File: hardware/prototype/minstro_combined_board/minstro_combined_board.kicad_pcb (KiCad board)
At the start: 4 copper layers, 130 x 100 mm, 89 parts, among them J301 BATT, J401 BOOT, J402 UART, J403 USB_C_Receptacle_USB2.0_16P, J404 SDMMC 4b, J405 Conn_Coaxial, J601 FT6236_Conn_01x06, J602 ILI9488_Conn, J603 ST7789_Conn_01x12, Q601 2N7002, SW401 RST, SW801 Navigation_Encoder_Joystick_S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, SW901 POWER, U201 LMR36006, U301 BQ24074RGT, U401 ESP32-S3, U402 W25Q128JVS, U701 ATSAMD10D13A-M, Y401 40 MHz

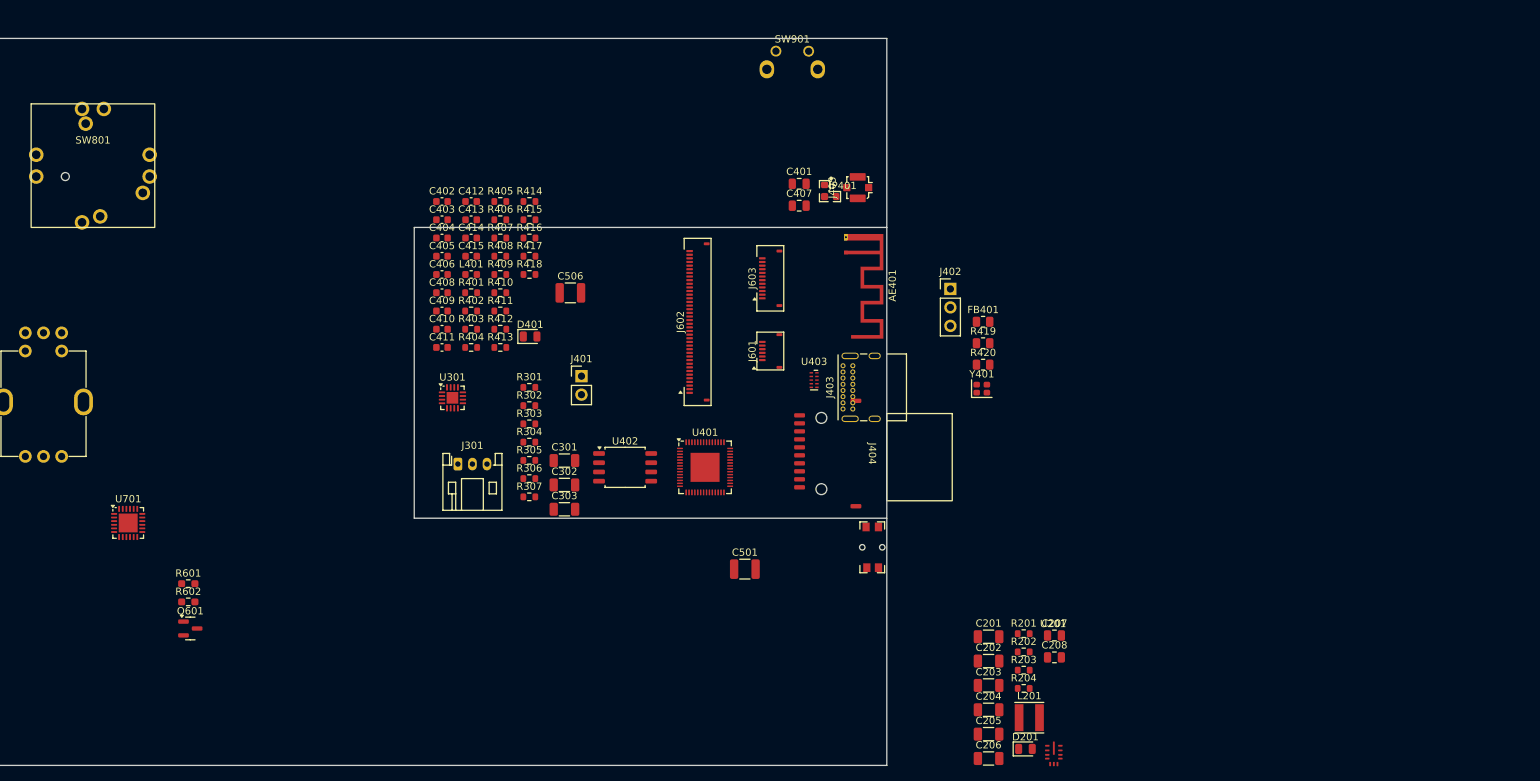
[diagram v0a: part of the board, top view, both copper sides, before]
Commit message: Footprint assignment and PCB layout work
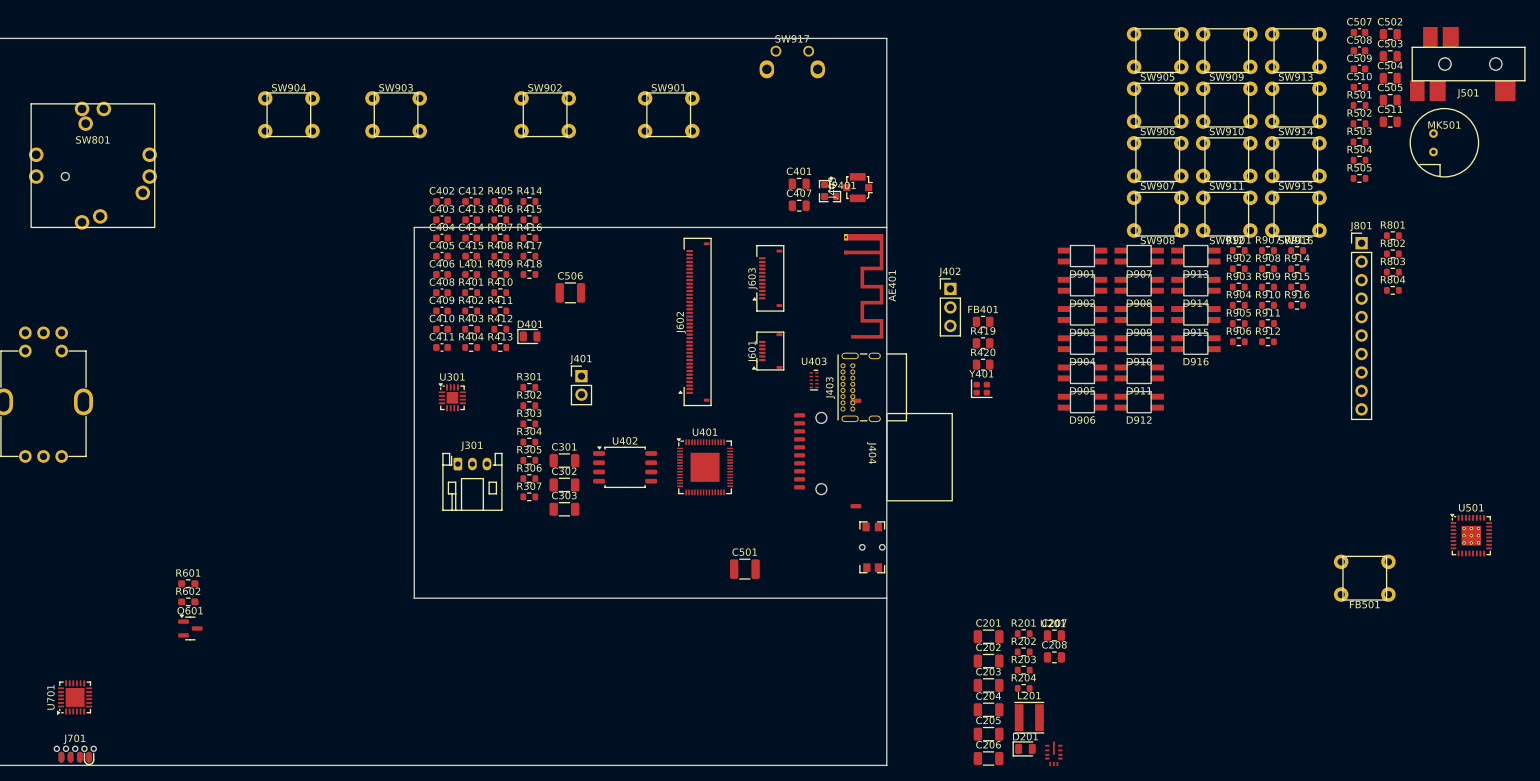
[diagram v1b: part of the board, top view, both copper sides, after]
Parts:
- added C502: 4.7uF, Capacitor_SMD:C_0805_2012Metric, F.Cu at (264.2, 39.4)
- added C503: 4.7uF, Capacitor_SMD:C_0805_2012Metric, F.Cu at (264.2, 42.4)
- added C504: 4.7uF, Capacitor_SMD:C_0805_2012Metric, F.Cu at (264.2, 45.5)
- added C505: 4.7uF, Capacitor_SMD:C_0805_2012Metric, F.Cu at (264.2, 48.5)
- added C507: 1uF, Capacitor_SMD:C_0603_1608Metric, F.Cu at (260.0, 39.2)
- added C508: 1uF, Capacitor_SMD:C_0603_1608Metric, F.Cu at (260.0, 41.7)
- added C509: 1uF, Capacitor_SMD:C_0603_1608Metric, F.Cu at (260.0, 44.2)
- added C510: 1uF, Capacitor_SMD:C_0603_1608Metric, F.Cu at (260.0, 46.7)
- added C511: 4.7uF, Capacitor_SMD:C_0805_2012Metric, F.Cu at (264.2, 51.5)
- added D901: ~, BVH_LED:SK6812Mini-E_Front, F.Cu at (221.9, 69.9)
- added D902: ~, BVH_LED:SK6812Mini-E_Front, F.Cu at (221.9, 74.0)
- added D903: ~, BVH_LED:SK6812Mini-E_Front, F.Cu at (221.9, 78.0)
- added D904: ~, BVH_LED:SK6812Mini-E_Front, F.Cu at (221.9, 82.0)
- added D905: ~, BVH_LED:SK6812Mini-E_Front, F.Cu at (221.9, 86.0)
- added D906: ~, BVH_LED:SK6812Mini-E_Front, F.Cu at (221.9, 90.0)
- added D907: ~, BVH_LED:SK6812Mini-E_Front, F.Cu at (229.7, 69.9)
- added D908: ~, BVH_LED:SK6812Mini-E_Front, F.Cu at (229.7, 74.0)
- added D909: ~, BVH_LED:SK6812Mini-E_Front, F.Cu at (229.7, 78.0)
- added D910: ~, BVH_LED:SK6812Mini-E_Front, F.Cu at (229.7, 82.0)
- added D911: ~, BVH_LED:SK6812Mini-E_Front, F.Cu at (229.7, 86.0)
- added D912: ~, BVH_LED:SK6812Mini-E_Front, F.Cu at (229.7, 90.0)
- added D913: ~, BVH_LED:SK6812Mini-E_Front, F.Cu at (237.5, 69.9)
- added D914: ~, BVH_LED:SK6812Mini-E_Front, F.Cu at (237.5, 74.0)
- added D915: ~, BVH_LED:SK6812Mini-E_Front, F.Cu at (237.5, 78.0)
- added D916: ~, BVH_LED:SK6812Mini-E_Front, F.Cu at (237.5, 82.0)
- added FB501: FerriteBead_Small, BVH_Switches:TacButton_6mm_6mm, F.Cu at (260.8, 114.2)
- added J501: Headset, BVH_Connectors_Misc:SJ-43515RS-SMT-TR, F.Cu at (275.0, 43.5)
- added J701: SOICbite-SWD, BVH_SOICbite:SOICbite_renumbered, F.Cu at (83.4, 140.0)
- added J801: Conn_01x10, Connector_PinHeader_2.54mm:PinHeader_1x10_P2.54mm_Vertical, F.Cu at (260.3, 68.2)
- added MK501: Microphone, BVH_Audio:SameSky_CMB-6544PF_Electret_Mic_9.4d, F.Cu at (271.7, 54.4)
- added R501: 100k, Resistor_SMD:R_0603_1608Metric, F.Cu at (260.0, 49.2)
- added R502: 100k, Resistor_SMD:R_0603_1608Metric, F.Cu at (260.0, 51.7)
- added R503: 220k, Resistor_SMD:R_0603_1608Metric, F.Cu at (260.0, 54.2)
- added R504: 2.2k, Resistor_SMD:R_0603_1608Metric, F.Cu at (260.0, 56.8)
- added R505: 2.2k, Resistor_SMD:R_0603_1608Metric, F.Cu at (260.0, 59.3)
- added R801: R_1, Resistor_SMD:R_0603_1608Metric, F.Cu at (264.6, 67.1)
- added R802: R_2, Resistor_SMD:R_0603_1608Metric, F.Cu at (264.6, 69.6)
- added R803: R_3, Resistor_SMD:R_0603_1608Metric, F.Cu at (264.6, 72.2)
- added R804: R_4, Resistor_SMD:R_0603_1608Metric, F.Cu at (264.6, 74.7)
- added R901: R_1, Resistor_SMD:R_0603_1608Metric, F.Cu at (243.4, 69.2)
- added R902: R_2, Resistor_SMD:R_0603_1608Metric, F.Cu at (243.4, 71.7)
- added R903: R_3, Resistor_SMD:R_0603_1608Metric, F.Cu at (243.4, 74.2)
- added R904: R_4, Resistor_SMD:R_0603_1608Metric, F.Cu at (243.4, 76.7)
- added R905: R_1, Resistor_SMD:R_0603_1608Metric, F.Cu at (243.4, 79.2)
- added R906: R_2, Resistor_SMD:R_0603_1608Metric, F.Cu at (243.4, 81.7)
- added R907: R_3, Resistor_SMD:R_0603_1608Metric, F.Cu at (247.4, 69.2)
- added R908: R_4, Resistor_SMD:R_0603_1608Metric, F.Cu at (247.4, 71.7)
- added R909: R_1, Resistor_SMD:R_0603_1608Metric, F.Cu at (247.4, 74.2)
- added R910: R_2, Resistor_SMD:R_0603_1608Metric, F.Cu at (247.4, 76.7)
- added R911: R_3, Resistor_SMD:R_0603_1608Metric, F.Cu at (247.4, 79.2)
- added R912: R_4, Resistor_SMD:R_0603_1608Metric, F.Cu at (247.4, 81.7)
- added R913: R_1, Resistor_SMD:R_0603_1608Metric, F.Cu at (251.4, 69.2)
- added R914: R_2, Resistor_SMD:R_0603_1608Metric, F.Cu at (251.4, 71.7)
- added R915: R_3, Resistor_SMD:R_0603_1608Metric, F.Cu at (251.4, 74.2)
- added R916: R_4, Resistor_SMD:R_0603_1608Metric, F.Cu at (251.4, 76.7)
- added SW901: SW_A1, BVH_Switches:TacButton_6mm_6mm, F.Cu at (165.0, 50.5)
- added SW902: SW_A2, BVH_Switches:TacButton_6mm_6mm, F.Cu at (148.0, 50.5)
- added SW903: SW_A3, BVH_Switches:TacButton_6mm_6mm, F.Cu at (127.5, 50.5)
- added SW904: SW_A4, BVH_Switches:TacButton_6mm_6mm, F.Cu at (112.8, 50.5)
- added SW905: SW_B1, BVH_Switches:TacButton_6mm_6mm, F.Cu at (232.3, 41.7)
- added SW906: SW_B2, BVH_Switches:TacButton_6mm_6mm, F.Cu at (232.3, 49.2)
- added SW907: SW_B3, BVH_Switches:TacButton_6mm_6mm, F.Cu at (232.3, 56.7)
- added SW908: SW_B4, BVH_Switches:TacButton_6mm_6mm, F.Cu at (232.3, 64.2)
- added SW909: SW_C1, BVH_Switches:TacButton_6mm_6mm, F.Cu at (241.8, 41.7)
- added SW910: SW_C2, BVH_Switches:TacButton_6mm_6mm, F.Cu at (241.8, 49.2)
- added SW911: SW_C3, BVH_Switches:TacButton_6mm_6mm, F.Cu at (241.8, 56.7)
- added SW912: SW_C4, BVH_Switches:TacButton_6mm_6mm, F.Cu at (241.8, 64.2)
- added SW913: SW_D1, BVH_Switches:TacButton_6mm_6mm, F.Cu at (251.3, 41.7)
- added SW914: SW_D2, BVH_Switches:TacButton_6mm_6mm, F.Cu at (251.3, 49.2)
- added SW915: SW_D3, BVH_Switches:TacButton_6mm_6mm, F.Cu at (251.3, 56.7)
- added SW916: SW_D4, BVH_Switches:TacButton_6mm_6mm, F.Cu at (251.3, 64.2)
- added U501: ~, BVH_Package_QFN:QFN-32-1EP_5x5mm_P0.5mm_EP2.7x2.7mm_ThermalVias, F.Cu at (275.4, 108.4)
- moved U701 25.1 mm to (83.3, 130.7), turned to 90 degrees
- renumbered SW901 to SW917
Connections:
- J403 pad A4: /ESP32 Microcontroller/V_usb -> /Battery/Vusb
- J403 pad A9: /ESP32 Microcontroller/V_usb -> /Battery/Vusb
- J403 pad B4: /ESP32 Microcontroller/V_usb -> /Battery/Vusb
- J403 pad B9: /ESP32 Microcontroller/V_usb -> /Battery/Vusb
- J404 pad 11: unconnected-(J404-SHIELD-Pad11) -> GND
- J601 pad 2: /Display Connectors/DISP_TS_SDA -> /I2C_SDA
- J601 pad 3: /Display Connectors/DISP_TS_SCL -> /I2C_SCL
- R419 pad 1: /ESP32 Microcontroller/I2C_SDA -> /I2C_SDA
- R420 pad 1: /ESP32 Microcontroller/I2C_SCK -> /I2C_SCL
- S1001 pad 1: /HMI VFO/VFO_A -> /HMI Controller/VFO_A
- S1001 pad 3: /HMI VFO/VFO_B -> /HMI Controller/VFO_B
- S1001 pad 5: /HMI VFO/VFO_SW -> /HMI Controller/VFO_SW
- S1001 pad 6: /HMI VFO/VFO_ADJ_B -> /HMI Controller/VFO_ADJ_B
- S1001 pad 8: /HMI VFO/VFO_ADJ_A -> /HMI Controller/VFO_ADJ_A
- SW801 pad 1: /Nav Switch/NAV_A -> /HMI Controller/NAV_A
- SW801 pad 10: unconnected-(SW801-GND-Pad10) -> GND
- SW801 pad 2: /Nav Switch/NAV_B -> /HMI Controller/NAV_B
- SW801 pad 4: /Nav Switch/NAV_SW -> /HMI Controller/NAV_SW
- SW917 pad 1: /HMI Keypad/POW_SW -> /HMI Controller/POW_SW
- U401 pad 11: /ESP32 Microcontroller/I2C_SDA -> /I2C_SDA
- U401 pad 12: /ESP32 Microcontroller/I2C_SCK -> /I2C_SCL
- U401 pad 13: /ESP32 Microcontroller/DISP_DC -> /Display Connectors/DISP_DC
- U401 pad 14: /ESP32 Microcontroller/DISP_CS -> /Display Connectors/DISP_CS
- U401 pad 15: /ESP32 Microcontroller/DISP_SCL -> /Display Connectors/DISP_SCL
- U401 pad 16: /ESP32 Microcontroller/DISP_SDA -> /Display Connectors/DISP_SDA
- U401 pad 17: /ESP32 Microcontroller/DISP_RST -> /Display Connectors/DISP_RST
- U401 pad 18: /ESP32 Microcontroller/DISP_TS_INT -> /Display Connectors/DISP_TS_INT
- U401 pad 19: /ESP32 Microcontroller/DISP_TS_RST -> /Display Connectors/DISP_TS_RST
- U401 pad 21: /ESP32 Microcontroller/PWR_CHRG -> /Battery/PWR_CHRG
- U401 pad 22: /ESP32 Microcontroller/PWR_EXT -> /Battery/PWR_GOOD
- U401 pad 27: /ESP32 Microcontroller/DISP_BL -> /Display Connectors/DISP_BL
- U401 pad 38: /ESP32 Microcontroller/I2S_FS -> /Audio/I2S_FS
- U401 pad 39: /ESP32 Microcontroller/I2S_BCLK -> /Audio/I2S_BCLK
- U401 pad 40: /ESP32 Microcontroller/I2S_ADCOUT -> /Audio/I2S_ADCOUT
- U401 pad 41: /ESP32 Microcontroller/I2S_ADCIN -> /Audio/I2S_ADCIN
- U401 pad 42: /ESP32 Microcontroller/I2S_MCLK -> /Audio/I2S_MCLK
- U401 pad 52: /ESP32 Microcontroller/SD_CS -> /ESP32 Microcontroller/SD_DET
- U701 pad 15: /HMI Controller/SDA -> /I2C_SDA
- U701 pad 16: /HMI Controller/SCL -> /I2C_SCL
- U701 pad 21: /HMI Controller/INT -> /ESP32 Microcontroller/HMI_INT
- U701 pad 22: /HMI Controller/WAKE -> /ESP32 Microcontroller/HMI_WAKE
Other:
- outline, holes or cut-outs redrawn

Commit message: Layout WIP
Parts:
- removed D901, D902, D903, D904, D905, D906, D907, D908, D909, D910, D911, D912, D913, D914, D915, D916: ~, BVH_LED:SK6812Mini-E_Front
- removed R901, R905, R909, R913: R_1, Resistor_SMD:R_0603_1608Metric
- removed R902, R906, R910, R914: R_2, Resistor_SMD:R_0603_1608Metric
- removed R903, R907, R911, R915: R_3, Resistor_SMD:R_0603_1608Metric
- removed R904, R908, R912, R916: R_4, Resistor_SMD:R_0603_1608Metric
- removed SW901: SW_A1, BVH_Switches:TacButton_6mm_6mm
- removed SW902: SW_A2, BVH_Switches:TacButton_6mm_6mm
- removed SW903: SW_A3, BVH_Switches:TacButton_6mm_6mm
- removed SW904: SW_A4, BVH_Switches:TacButton_6mm_6mm
- removed SW905: SW_B1, BVH_Switches:TacButton_6mm_6mm
- removed SW906: SW_B2, BVH_Switches:TacButton_6mm_6mm
- removed SW907: SW_B3, BVH_Switches:TacButton_6mm_6mm
- removed SW908: SW_B4, BVH_Switches:TacButton_6mm_6mm
- removed SW909: SW_C1, BVH_Switches:TacButton_6mm_6mm
- removed SW910: SW_C2, BVH_Switches:TacButton_6mm_6mm
- removed SW911: SW_C3, BVH_Switches:TacButton_6mm_6mm
- removed SW912: SW_C4, BVH_Switches:TacButton_6mm_6mm
- removed SW913: SW_D1, BVH_Switches:TacButton_6mm_6mm
- removed SW914: SW_D2, BVH_Switches:TacButton_6mm_6mm
- removed SW915: SW_D3, BVH_Switches:TacButton_6mm_6mm
- removed SW916: SW_D4, BVH_Switches:TacButton_6mm_6mm
- added H101: MountingHole_Pad_MP, MountingHole:MountingHole_3.2mm_M3_Pad, F.Cu at (190.0, 45.0)
- added H102: MountingHole_Pad_MP, MountingHole:MountingHole_3.2mm_M3_Pad, F.Cu at (70.0, 45.0)
- added H103: MountingHole_Pad_MP, MountingHole:MountingHole_3.2mm_M3_Pad, F.Cu at (190.0, 135.5)
- added H104: MountingHole_Pad_MP, MountingHole:MountingHole_3.2mm_M3_Pad, F.Cu at (74.0, 133.5)
- added J1001: VFO, Connector_PinHeader_2.54mm:PinHeader_1x06_P2.54mm_Vertical, F.Cu at (72.0, 60.9)
- added S901: A1, BVH_Switches:TacButton_6mm_6mm_SK6812-E-Mini, F.Cu at (120.5, 51.0)
- added S902: A2, BVH_Switches:TacButton_6mm_6mm_SK6812-E-Mini, F.Cu at (140.1, 51.0)
- added S903: A3, BVH_Switches:TacButton_6mm_6mm_SK6812-E-Mini, F.Cu at (159.7, 51.0)
- added S904: A4, BVH_Switches:TacButton_6mm_6mm_SK6812-E-Mini, F.Cu at (185.5, 50.0)
- added S905: B1, BVH_Switches:TacButton_6mm_6mm_SK6812-E-Mini, F.Cu at (103.0, 70.0)
- added S906: B2, BVH_Switches:TacButton_6mm_6mm_SK6812-E-Mini, F.Cu at (103.0, 85.2)
- added S907: B3, BVH_Switches:TacButton_6mm_6mm_SK6812-E-Mini, F.Cu at (103.0, 100.3)
- added S908: B4, BVH_Switches:TacButton_6mm_6mm_SK6812-E-Mini, F.Cu at (103.0, 115.5)
- added S909: C1, BVH_Switches:TacButton_6mm_6mm_SK6812-E-Mini, F.Cu at (121.0, 129.8)
- added S910: C2, BVH_Switches:TacButton_6mm_6mm_SK6812-E-Mini, F.Cu at (141.0, 129.8)
- added S911: C3, BVH_Switches:TacButton_6mm_6mm_SK6812-E-Mini, F.Cu at (161.0, 129.8)
- added S912: C4, BVH_Switches:TacButton_6mm_6mm_SK6812-E-Mini, F.Cu at (181.0, 129.8)
- AE401: value Antenna_Shield -> ANT; footprint RF_Antenna:Texas_SWRA117D_2.4GHz_Right -> BVH_RF_Ham:ANT2012LL13R2400A
- FB501: footprint BVH_Switches:TacButton_6mm_6mm -> Resistor_SMD:R_0805_2012Metric
- J801: value Conn_01x10 -> NAV CONN
- moved J801 196.7 mm to (68.2, 110.5)
- moved R801 187.9 mm to (82.6, 113.8)
- moved R802 187.9 mm to (82.6, 116.3)
- moved R803 187.9 mm to (82.6, 118.8)
- moved R804 187.9 mm to (82.6, 121.3)
- moved MK501 184.6 mm to (102.0, 127.0), turned to 180 degrees
- moved C507 125.4 mm to (167.0, 123.2), turned to 90 degrees
- moved C505 122.8 mm to (163.0, 118.0), turned to 180 degrees
- moved C508 121.8 mm to (169.5, 123.2), turned to 90 degrees
- moved C504 120.6 mm to (167.5, 117.5), turned to -90 degrees
- moved C502 119.5 mm to (165.1, 106.0), turned to 180 degrees
- moved C503 114.9 mm to (168.5, 106.0)
- moved C511 114.7 mm to (170.5, 117.5), turned to -90 degrees
- moved C509 114.2 mm to (172.5, 117.5), turned to -90 degrees
- moved J501 112.3 mm to (187.2, 113.5), turned to 180 degrees
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- renumbered SW917 to S917
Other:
- outline, holes or cut-outs redrawn
